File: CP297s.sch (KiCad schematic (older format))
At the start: 110 parts, among them J1 Conn_01x05_Male, J2 Conn_01x04_Female, J3 pin header 01x15 2.54mm, J4 Conn_01x06_Female, J5 RCA-103, J6 PJ-301M, J7 PJ-301M, K1 CONN_3, K2 CONN_3, K3 TK85_BUS, P2 CONN_2, P6 CONN_2, U1 Z80, U10 74LS125, U11 74LS393, U12 74LS574, U13 74LS08, U14 74LS251, U15 74HC86, U16 74LS245, U17 74LS32, U18 74HCT00, U19 74LS138, U2 62256, U20 74HC74, U21 74HC74, U22 74LS165, U23 74LS32, U25 74LS08, U3 27256, U4 74HC04, U5 74HC74, U6 74LS393, U7 74LS11, U8 74LS32, U9 74LS245, X1 6.5MHz

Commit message: add PSG, changed AV connectors
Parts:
- removed J5: RCA-103, CP297s:RCA-103, symbol CP297s:Conn_Coaxial-Connector
- removed J6, J7: PJ-301M, CP297s:PJ-301M, symbol CP297s:PJ-301M
- added C26, C27: 100n, Capacitor_THT:C_Disc_D7.0mm_W2.5mm_P5.00mm, symbol CP297s:C-CP297s
- added C28, C29: 1uF, Capacitor_THT:CP_Radial_D5.0mm_P2.50mm, symbol CP297s:CAPAPOL-CP297s
- added J5, J6, J7: PG203J, CP297s:PG203J, symbol Connector_Specialized:Audio-Jack-3_2Switches
- added R37, R40: 1k, Resistor_THT:R_Axial_DIN0207_L6.3mm_D2.5mm_P7.62mm_Horizontal, symbol CP297s:R-CP297s
- added R38, R39, R41, R42: 2k2, Resistor_THT:R_Axial_DIN0207_L6.3mm_D2.5mm_P7.62mm_Horizontal, symbol CP297s:R-CP297s
- added unit 3 of U10
- added unit 2 of U11
- added unit 4 of U15
- added U24: AY-3-8910, Package_DIP:DIP-40_W15.24mm, symbol CP297s:AY-3-8910
- added U26: 74LS138, Package_DIP:DIP-16_W7.62mm, symbol CP297s:74LS138-CP297s
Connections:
- net labels added: 1.625MHz, AUDIO-L, AUDIO-MONO, AUDIO-R, ~IOWR
- wire segments 754 -> 843
- no-connect marks 19 -> 49
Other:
- note added: "A/V\nOUT"
- note added: "BORDER"
- note added: "EAR/MIC"
- note removed: "EAR"
- note removed: "MIC"
- moved on the sheet: BT1, C10, C11, C12, C13, C14, C15, C16, C17, C19, C21, C22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

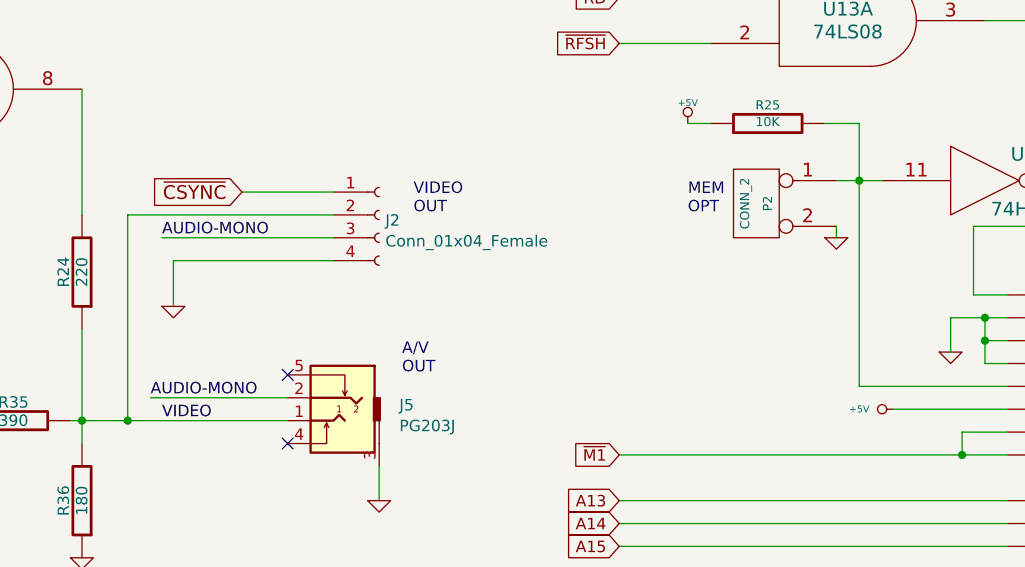
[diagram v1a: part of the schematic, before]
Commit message: moved battery clip, substituted audio-mono for +5Vcc at MONITOR OUT connector
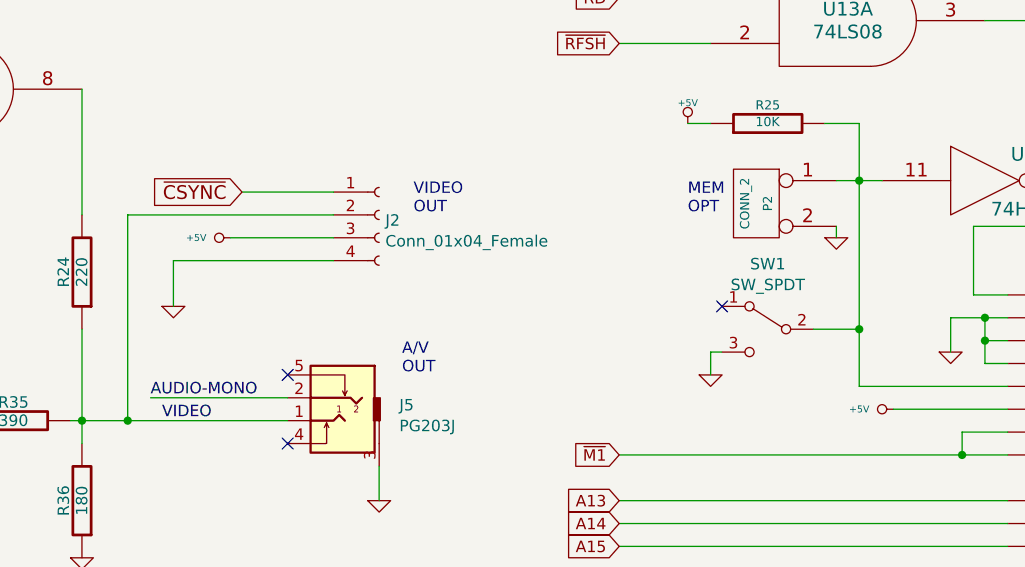
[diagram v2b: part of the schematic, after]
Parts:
- added SW1: SW_SPDT, Button_Switch_THT:SW_CuK_OS102011MA1QN1_SPDT_Angled, symbol Switch:SW_SPDT
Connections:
- net +5V: now also J2.3 (Pin_3)
- net AUDIO-MONO: no longer J2.3 (Pin_3)
- net GND: now also SW1.3 (C)
- net at P2.1 (P1), R25.2, U14.15 (I4)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: now also SW1.2 (B)
- no-connect marks 49 -> 50
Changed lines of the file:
@@
 	11550 12800 11650 12800
 Wire Wire Line
-	11550 12800 11550 13700
+	11550 12800 11550 13450
 Wire Wire Line
 	12100 13400 12200 13400
@@
 	8500 17700 8900 17700
 Wire Wire Line
-	9250 13050 8500 13050
-Text Label 8500 13050 0    50   ~ 0
-AUDIO-MONO
+	9250 13050 8800 13050
 $Comp
 L CP297s:R-CP297s R38
@@
 NoConn ~ 13900 20600
 NoConn ~ 13900 20300
+$Comp
+L Switch:SW_SPDT SW1
+U 1 1 5D3DC721
+P 11150 13450
+F 0 "SW1" H 11150 13735 50  0000 C CNN
+F 1 "SW_SPDT" H 11150 13644 50  0000 C CNN
+F 2 "Button_Switch_THT:SW_CuK_OS102011MA1QN1_SPDT_Angled" H 11150 13450 50  0001 C CNN
+F 3 "" H 11150 13450 50  0001 C CNN
+	1    11150 13450
+	-1   0    0    -1
+$EndComp
+$Comp
+L CP297s:GND-CP297s #PWR035
+U 1 1 5D3ECC23
+P 10900 13650
+F 0 "#PWR035" H 10900 13650 30  0001 C CNN
+F 1 "GND" H 10900 13580 30  0001 C CNN
+F 2 "" H 10900 13650 60  0000 C CNN
+F 3 "" H 10900 13650 60  0000 C CNN
+	1    10900 13650
+	1    0    0    -1
+$EndComp
+Wire Wire Line
+	11350 13450 11550 13450
+Connection ~ 11550 13450
+Wire Wire Line
+	11550 13450 11550 13700
+Wire Wire Line
+	10950 13550 10900 13550
+Wire Wire Line
+	10900 13550 10900 13650
+NoConn ~ 10950 13350
+$Comp
+L CP297s:+5V-CP297s #PWR?
+U 1 1 5D43F284
+P 8800 13050
+F 0 "#PWR?" H 8800 13140 20  0001 C CNN
+F 1 "+5V" V 8800 13200 30  0000 C CNN
+F 2 "" H 8800 13050 60  0000 C CNN
+F 3 "" H 8800 13050 60  0000 C CNN
+	1    8800 13050
+	0    -1   -1   0
+$EndComp
 $EndSCHEMATC

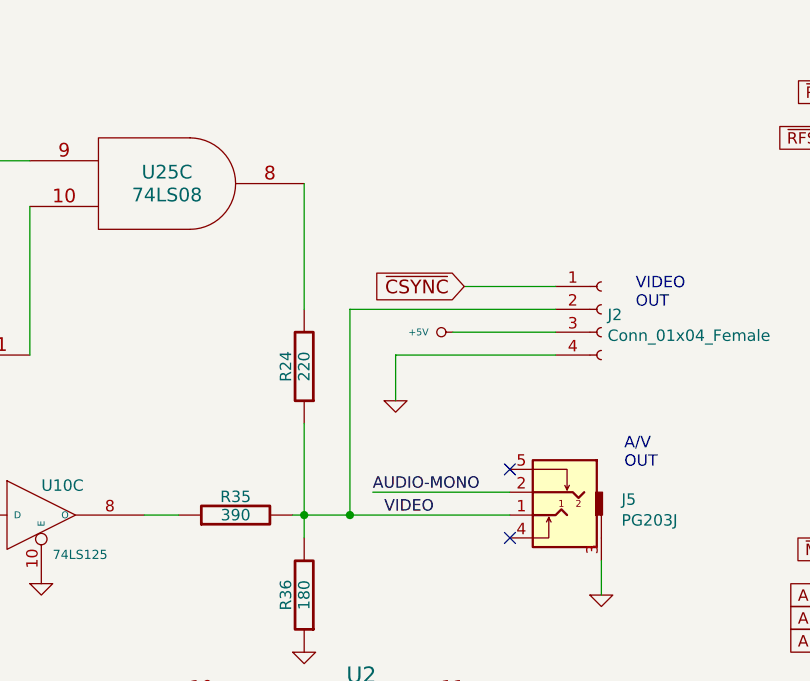
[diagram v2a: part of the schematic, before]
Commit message: updated board outline, support for external kolour
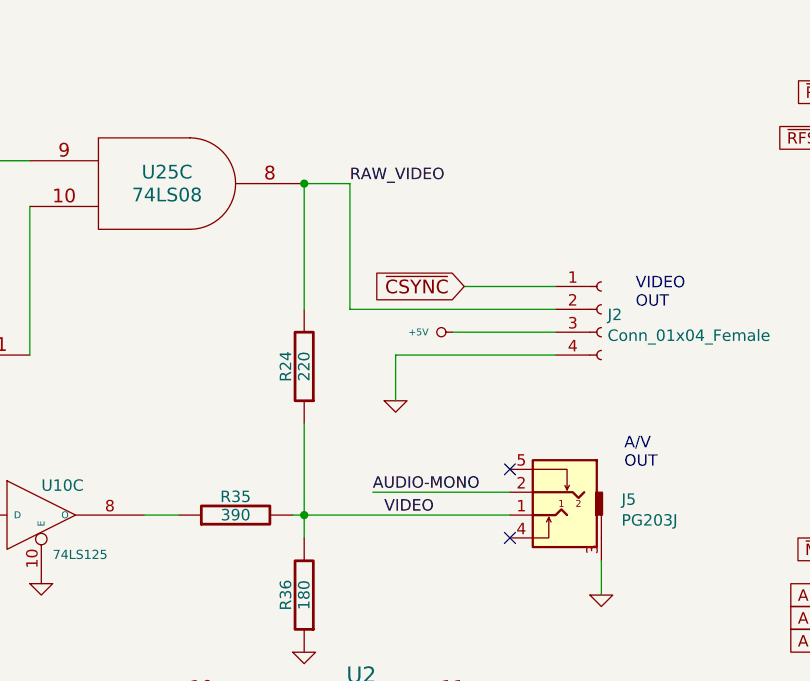
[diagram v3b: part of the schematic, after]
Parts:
- SW1: footprint Button_Switch_THT:SW_CuK_OS102011MA1QN1_SPDT_Angled -> CP297s:SS-12F23_SPDT_Angled
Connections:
- net VIDEO: no longer J2.2 (Pin_2)
- net RAW_VIDEO: now reaches R24.2, U25.8
- net RAW_VIDEO: now also J2.2 (Pin_2)
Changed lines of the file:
@@
-EESchema Schematic File Version 4
+EESchema Schematic File Version 5
 LIBS:CP297s-cache
 EELAYER 29 0
@@
 	5100 12100 5400 12100
 Wire Wire Line
-	4150 10600 7800 10600
-Wire Wire Line
 	4150 10600 4150 11800
 Wire Wire Line
@@
 NoConn ~ 4550 21850
 Wire Wire Line
-	9050 13850 8350 13850
-Wire Wire Line
-	8350 13850 8350 12950
-Wire Wire Line
 	8350 12950 9250 12950
 $Comp
@@
 Wire Wire Line
 	8150 12400 8150 12950
-Wire Wire Line
-	8150 13850 8350 13850
-Connection ~ 8350 13850
 $Comp
 L CP297s:C-CP297s C22
@@
 F 0 "SW1" H 11150 13735 50  0000 C CNN
 F 1 "SW_SPDT" H 11150 13644 50  0000 C CNN
-F 2 "Button_Switch_THT:SW_CuK_OS102011MA1QN1_SPDT_Angled" H 11150 13450 50  0001 C CNN
+F 2 "CP297s:SS-12F23_SPDT_Angled" H 11150 13450 50  0001 C CNN
 F 3 "" H 11150 13450 50  0001 C CNN
 	1    11150 13450
@@
 NoConn ~ 10950 13350
 $Comp
-L CP297s:+5V-CP297s #PWR?
+L CP297s:+5V-CP297s #PWR0110
 U 1 1 5D43F284
 P 8800 13050
-F 0 "#PWR?" H 8800 13140 20  0001 C CNN
+F 0 "#PWR0110" H 8800 13140 20  0001 C CNN
 F 1 "+5V" V 8800 13200 30  0000 C CNN
 F 2 "" H 8800 13050 60  0000 C CNN
@@
 	0    -1   -1   0
 $EndComp
+Wire Wire Line
+	4150 10600 7800 10600
+Wire Wire Line
+	8150 12400 8350 12400
+Wire Wire Line
+	8350 12400 8350 12950
+Connection ~ 8150 12400
+Wire Wire Line
+	8150 13850 9050 13850
+Text Label 8350 12400 0    50   ~ 0
+RAW_VIDEO
 $EndSCHEMATC

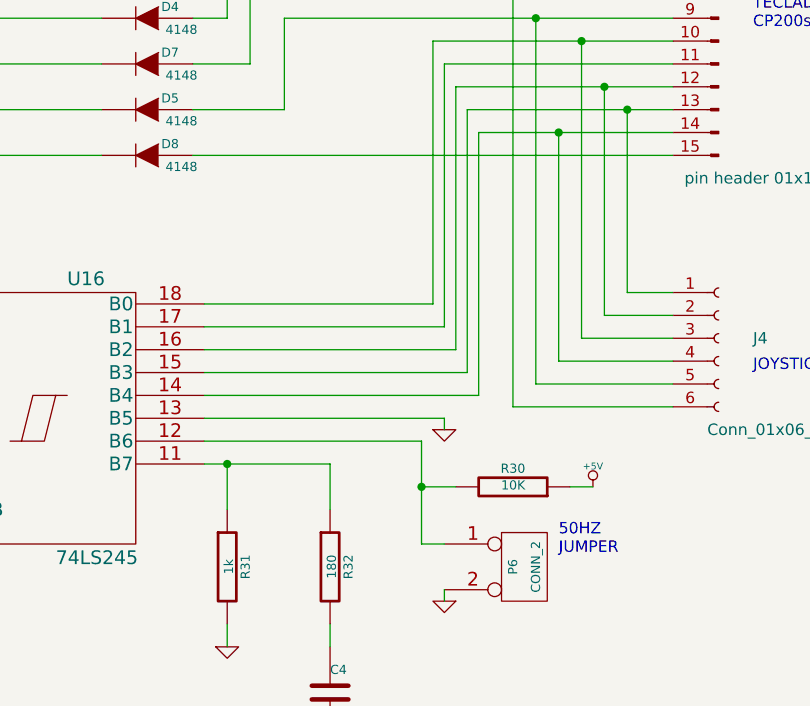
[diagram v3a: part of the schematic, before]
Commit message: Added resistor network at keyboard inputs
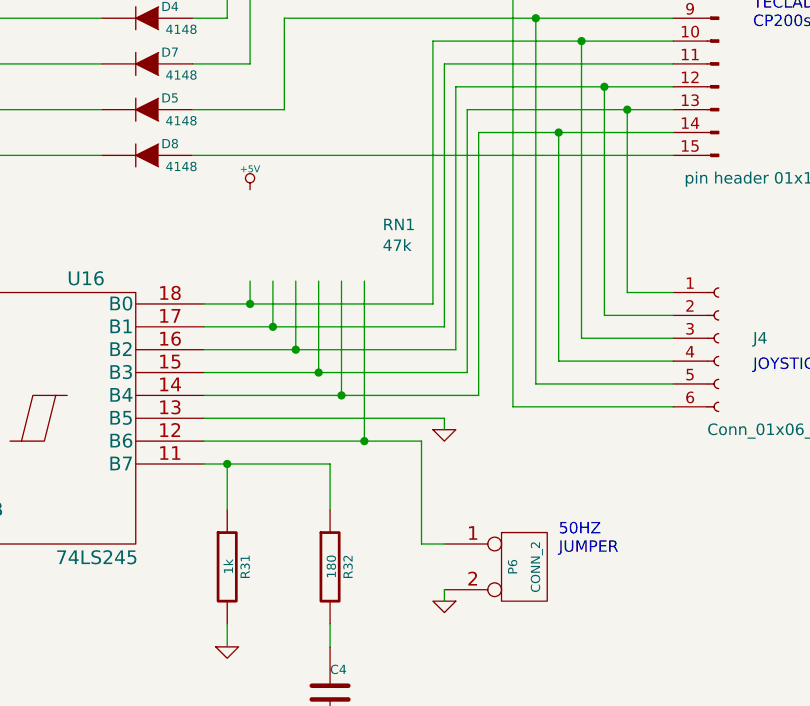
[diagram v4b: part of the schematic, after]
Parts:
- removed R30: 10K, Resistor_THT:R_Axial_DIN0207_L6.3mm_D2.5mm_P7.62mm_Horizontal, symbol CP297s:R-CP297s
- added RN1: 47k, Resistor_THT:R_Array_SIP7, symbol Device:R_Network06
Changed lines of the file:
@@
 $EndComp
 $Comp
-L CP297s:R-CP297s R30
-U 1 1 51BD6352
-P 14050 18850
-F 0 "R30" V 14130 18850 40  0000 C CNN
-F 1 "10K" V 14057 18851 40  0000 C CNN
-F 2 "Resistor_THT:R_Axial_DIN0207_L6.3mm_D2.5mm_P7.62mm_Horizontal" V 13980 18850 30  0001 C CNN
-F 3 "~" H 14050 18850 30  0001 C CNN
-	1    14050 18850
-	0    1    -1   0
-$EndComp
-$Comp
 L CP297s:GND-CP297s #PWR033
 U 1 1 51BD6358
@@
 	-1   0    0    -1
 $EndComp
-$Comp
-L CP297s:+5V-CP297s #PWR034
-U 1 1 51BD635E
-P 14400 18850
-F 0 "#PWR034" H 14400 18940 20  0001 C CNN
-F 1 "+5V" H 14400 18940 30  0000 C CNN
-F 2 "" H 14400 18850 60  0000 C CNN
-F 3 "" H 14400 18850 60  0000 C CNN
-	1    14400 18850
-	-1   0    0    -1
-$EndComp
 Text Notes 14250 19150 0    50   ~ 0
 50HZ\nJUMPER
@@
 	11300 18750 10500 18750
 Wire Wire Line
-	12700 18050 13700 18050
+	12700 18050 12900 18050
 Wire Wire Line
 	12700 18550 13750 18550
@@
 	13750 18550 13750 18600
 Wire Wire Line
-	13800 18850 13650 18850
-Wire Wire Line
 	13750 19300 13750 19350
 Wire Wire Line
-	14400 18850 14300 18850
-Wire Wire Line
 	13650 19100 13750 19100
 Wire Wire Line
-	13650 18650 13650 18850
-Wire Wire Line
-	12700 18650 13650 18650
-Connection ~ 13650 18850
+	12700 18650 13400 18650
 Wire Wire Line
 	12300 20400 12450 20400
@@
 	12050 6450 11550 6450
 Wire Wire Line
-	13650 18850 13650 19100
-Wire Wire Line
 	12800 18750 13250 18750
 Wire Wire Line
@@
 	13750 17000 13750 18150
 Wire Wire Line
-	12700 18150 13750 18150
+	12700 18150 13000 18150
 Wire Wire Line
 	14750 17100 14450 17100
@@
 	13800 17100 13800 18250
 Wire Wire Line
-	12700 18250 13800 18250
+	12700 18250 13100 18250
 Wire Wire Line
 	14750 17200 14550 17200
@@
 	13850 17200 13850 18350
 Wire Wire Line
-	12700 18350 13850 18350
+	12700 18350 13200 18350
 Wire Wire Line
 	14750 17300 14250 17300
@@
 	13900 17300 13900 18450
 Wire Wire Line
-	12700 18450 13900 18450
+	12700 18450 13300 18450
 Wire Wire Line
 	12900 16700 14750 16700
@@
 Text Label 8350 12400 0    50   ~ 0
 RAW_VIDEO
+$Comp
+L CP297s:+5V-CP297s #PWR0111
+U 1 1 5D4CAC77
+P 12900 17550
+F 0 "#PWR0111" H 12900 17640 20  0001 C CNN
+F 1 "+5V" H 12900 17640 30  0000 C CNN
+F 2 "" H 12900 17550 60  0000 C CNN
+F 3 "" H 12900 17550 60  0000 C CNN
+	1    12900 17550
+	-1   0    0    -1
+$EndComp
+Wire Wire Line
+	12900 17950 12900 18050
+Connection ~ 12900 18050
+Wire Wire Line
+	12900 18050 13700 18050
+Wire Wire Line
+	13000 17950 13000 18150
+Connection ~ 13000 18150
+Wire Wire Line
+	13000 18150 13750 18150
+Wire Wire Line
+	13100 17950 13100 18250
+Connection ~ 13100 18250
+Wire Wire Line
+	13100 18250 13800 18250
+Wire Wire Line
+	13200 17950 13200 18350
+Connection ~ 13200 18350
+Wire Wire Line
+	13200 18350 13850 18350
+Wire Wire Line
+	13300 17950 13300 18450
+Connection ~ 13300 18450
+Wire Wire Line
+	13300 18450 13900 18450
+$Comp
+L Device:R_Network06 RN1
+U 0 0 5D4DA09D
+P 13200 17750
+F 0 "RN1" H 13480 17796 50  0000 L CNN
+F 1 "47k" H 13480 17705 50  0000 L CNN
+F 2 "Resistor_THT:R_Array_SIP7" V 13575 17750 50  0001 C CNN
+F 3 "http://www.vishay.com/docs/31509/csc.pdf" H 13200 17750 50  0001 C CNN
+	0    13200 17750
+	1    0    0    -1
+$EndComp
+Wire Wire Line
+	13400 17950 13400 18650
+Connection ~ 13400 18650
+Wire Wire Line
+	13400 18650 13650 18650
+Wire Wire Line
+	13650 18650 13650 19100
 $EndSCHEMATC

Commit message: fixed CPU syncrhonizer (/wait logic)
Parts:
- added D12: 4148, Diode_THT:D_A-405_P7.62mm_Horizontal, symbol CP297s:DIODE-CP297s
- added R30: 10K, Resistor_THT:R_Axial_DIN0207_L6.3mm_D2.5mm_P7.62mm_Horizontal, symbol CP297s:R-CP297s
- D1: value DIODE -> 4148
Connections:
- net +5V: now also RN1.1 (common), R30.1
- net ~WAIT: now also D12.1 (A), R30.2; no longer U23.6
- net at P6.1 (P1), U16.12 (B6): now also RN1.7 (R6)
- net at J3.14 (Pin_14), J4.4 (Pin_4), U16.14 (B4): now also RN1.6 (R5)
- net at J3.13 (Pin_13), J4.1 (Pin_1), U16.15 (B3): now also RN1.5 (R4)
- net at J3.12 (Pin_12), J4.2 (Pin_2), U16.16 (B2): now also RN1.4 (R3)
- net at J3.11 (Pin_11), U16.17 (B1): now also RN1.3 (R2)
- net at J3.10 (Pin_10), J4.3 (Pin_3), U16.18 (B0): now also RN1.2 (R1)
- new net: D12.2 (K), U23.6
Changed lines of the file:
@@
 P 5350 13500
 F 0 "D1" H 5350 13600 40  0000 C CNN
-F 1 "DIODE" H 5350 13400 40  0000 C CNN
+F 1 "4148" H 5350 13400 40  0000 C CNN
 F 2 "Diode_THT:D_A-405_P7.62mm_Horizontal" H 5350 13500 60  0001 C CNN
 F 3 "" H 5350 13500 60  0001 C CNN
@@
 	1    0    0    -1
 $EndComp
-Text GLabel 14650 1600 2    50   Input ~ 0
+Text GLabel 15100 1600 2    50   Input ~ 0
 ~WAIT
 Text GLabel 12100 1500 0    50   Input ~ 0
@@
 	14450 4800 14450 4900
 Wire Wire Line
-	14450 1600 14650 1600
-Wire Wire Line
 	13250 1700 13150 1700
 Wire Wire Line
@@
 $Comp
 L Device:R_Network06 RN1
-U 0 0 5D4DA09D
+U 1 1 5D4DA09D
 P 13200 17750
 F 0 "RN1" H 13480 17796 50  0000 L CNN
@@
 F 2 "Resistor_THT:R_Array_SIP7" V 13575 17750 50  0001 C CNN
 F 3 "http://www.vishay.com/docs/31509/csc.pdf" H 13200 17750 50  0001 C CNN
-	0    13200 17750
+	1    13200 17750
 	1    0    0    -1
 $EndComp
@@
 Wire Wire Line
 	13650 18650 13650 19100
+$Comp
+L CP297s:DIODE-CP297s D12
+U 1 1 5D4F5956
+P 14650 1600
+F 0 "D12" H 14650 1700 40  0000 C CNN
+F 1 "4148" H 14650 1500 40  0000 C CNN
+F 2 "Diode_THT:D_A-405_P7.62mm_Horizontal" H 14650 1600 60  0001 C CNN
+F 3 "" H 14650 1600 60  0001 C CNN
+	1    14650 1600
+	-1   0    0    1
+$EndComp
+$Comp
+L CP297s:R-CP297s R30
+U 1 1 5D500071
+P 14900 1250
+F 0 "R30" V 14980 1250 40  0000 C CNN
+F 1 "10K" V 14907 1251 40  0000 C CNN
+F 2 "Resistor_THT:R_Axial_DIN0207_L6.3mm_D2.5mm_P7.62mm_Horizontal" V 14830 1250 30  0001 C CNN
+F 3 "~" H 14900 1250 30  0001 C CNN
+	1    14900 1250
+	1    0    0    -1
+$EndComp
+$Comp
+L CP297s:+5V-CP297s #PWR034
+U 1 1 5D508F33
+P 14900 1000
+F 0 "#PWR034" H 14900 1090 20  0001 C CNN
+F 1 "+5V" H 14900 1090 30  0000 C CNN
+F 2 "" H 14900 1000 60  0000 C CNN
+F 3 "" H 14900 1000 60  0000 C CNN
+	1    14900 1000
+	1    0    0    -1
+$EndComp
+Wire Wire Line
+	14850 1600 14900 1600
+Wire Wire Line
+	14900 1600 14900 1500
+Wire Wire Line
+	14900 1600 15100 1600
+Connection ~ 14900 1600
 $EndSCHEMATC
